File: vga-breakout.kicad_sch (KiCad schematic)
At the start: 8 parts, among them J1 DE15_Socket_HighDensity_Mount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, J2 Conn_01x11_Pin, J3 USB_C_Receptacle_PowerOnly_6P, SW1 SW_SPDT_321

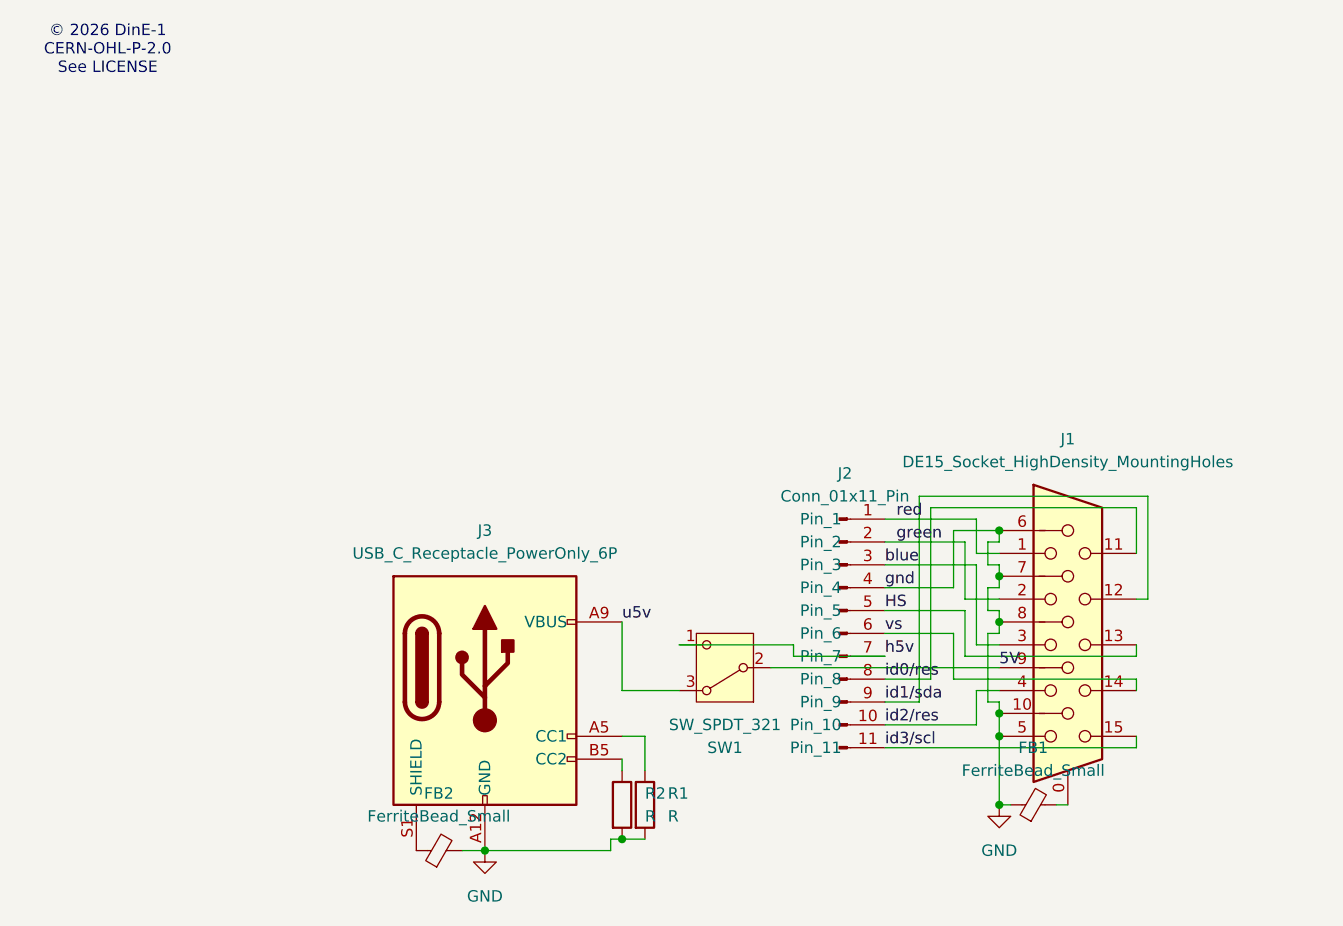
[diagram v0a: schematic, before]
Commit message: remove ferrite from sheilding, rerouting
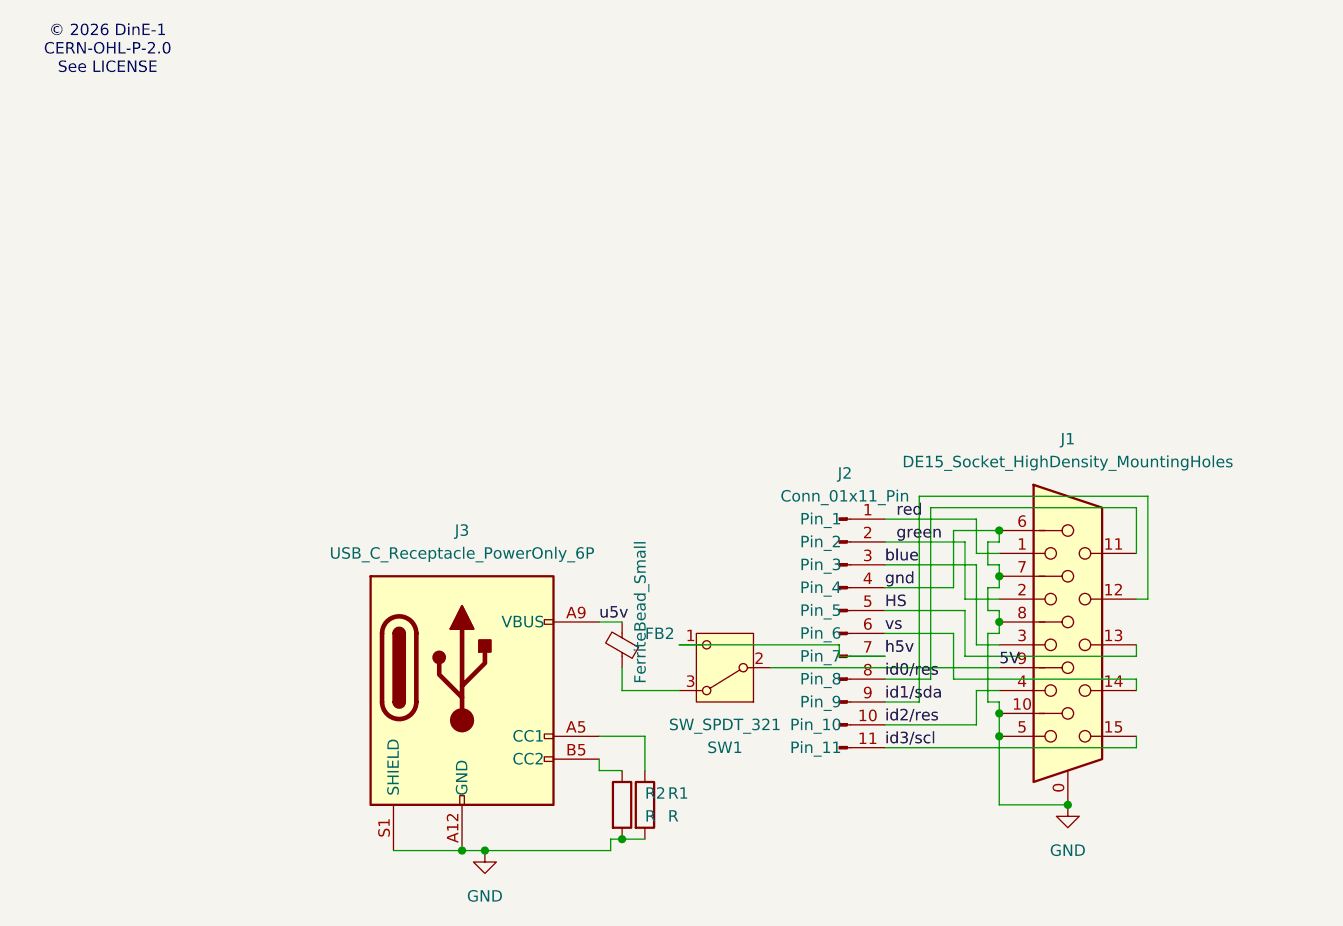
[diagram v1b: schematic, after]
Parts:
- removed FB1: FerriteBead_Small, Inductor_SMD:L_0805_2012Metric, symbol Device:FerriteBead_Small
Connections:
- net GND: now also J1.0, J3.S1 (SHIELD); no longer FB2.2
- net u5v: now also FB2.2; no longer SW1.3 (A)
- net at FB2.1: now also SW1.3 (A); no longer J3.S1 (SHIELD)
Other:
- moved on the sheet: FB2, J3

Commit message: add tvs diode, reroute
reroute with vias only for 5V trace
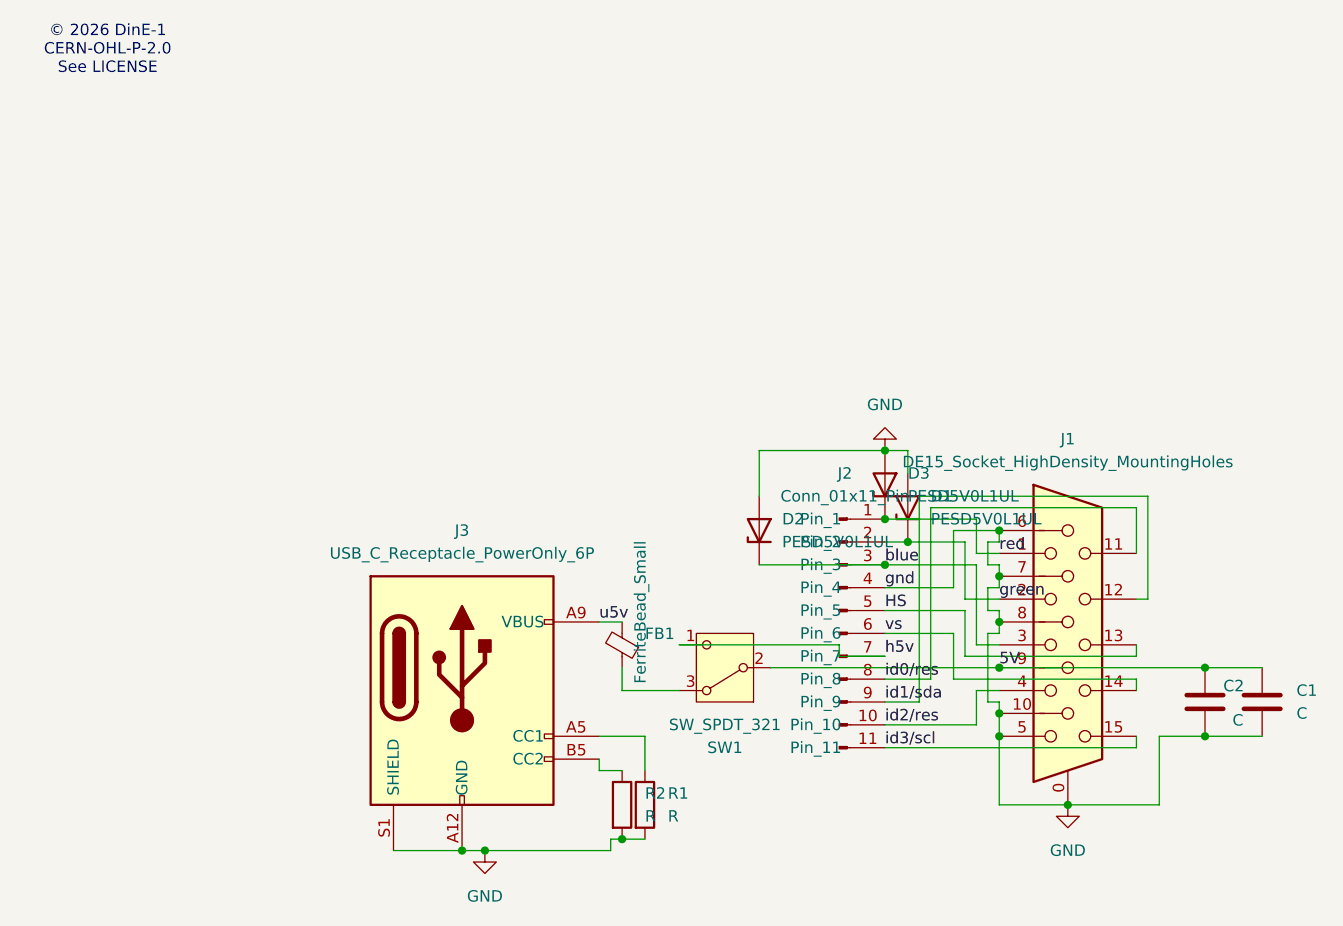
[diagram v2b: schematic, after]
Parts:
- added C1, C2: C, Capacitor_SMD:C_0603_1608Metric, symbol Device:C
- added D1, D2, D3: PESD5V0L1UL, Diode_SMD:D_SOD-882, symbol Diode:PESD5V0L1UL
- renumbered FB2 to FB1
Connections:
- net 5V: now also C1.1, C2.1
- net GND: now also C1.2, C2.2, D1.2 (A), D2.2 (A), D3.2 (A)
- net blue: now also D2.1 (K)
- net green: now also D1.1 (K)
- net red: now also D3.1 (K)
